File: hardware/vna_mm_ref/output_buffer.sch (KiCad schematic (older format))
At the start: 35 parts, among them J201 Conn_Coaxial, J202 Conn_Coaxial, U201 LTC6957xDD-3

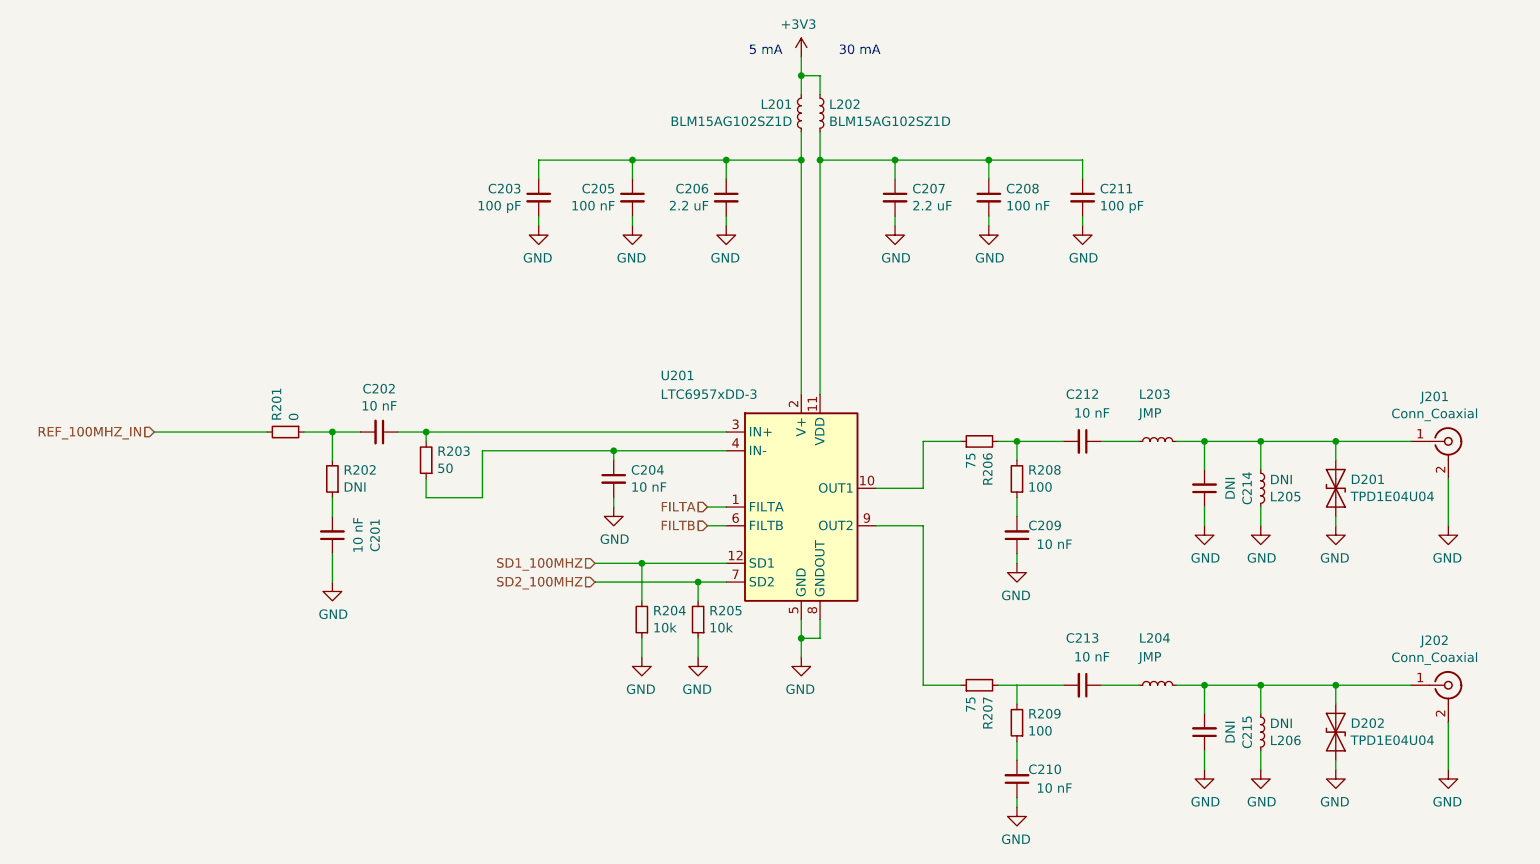
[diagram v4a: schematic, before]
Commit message: component placement on vna ref board
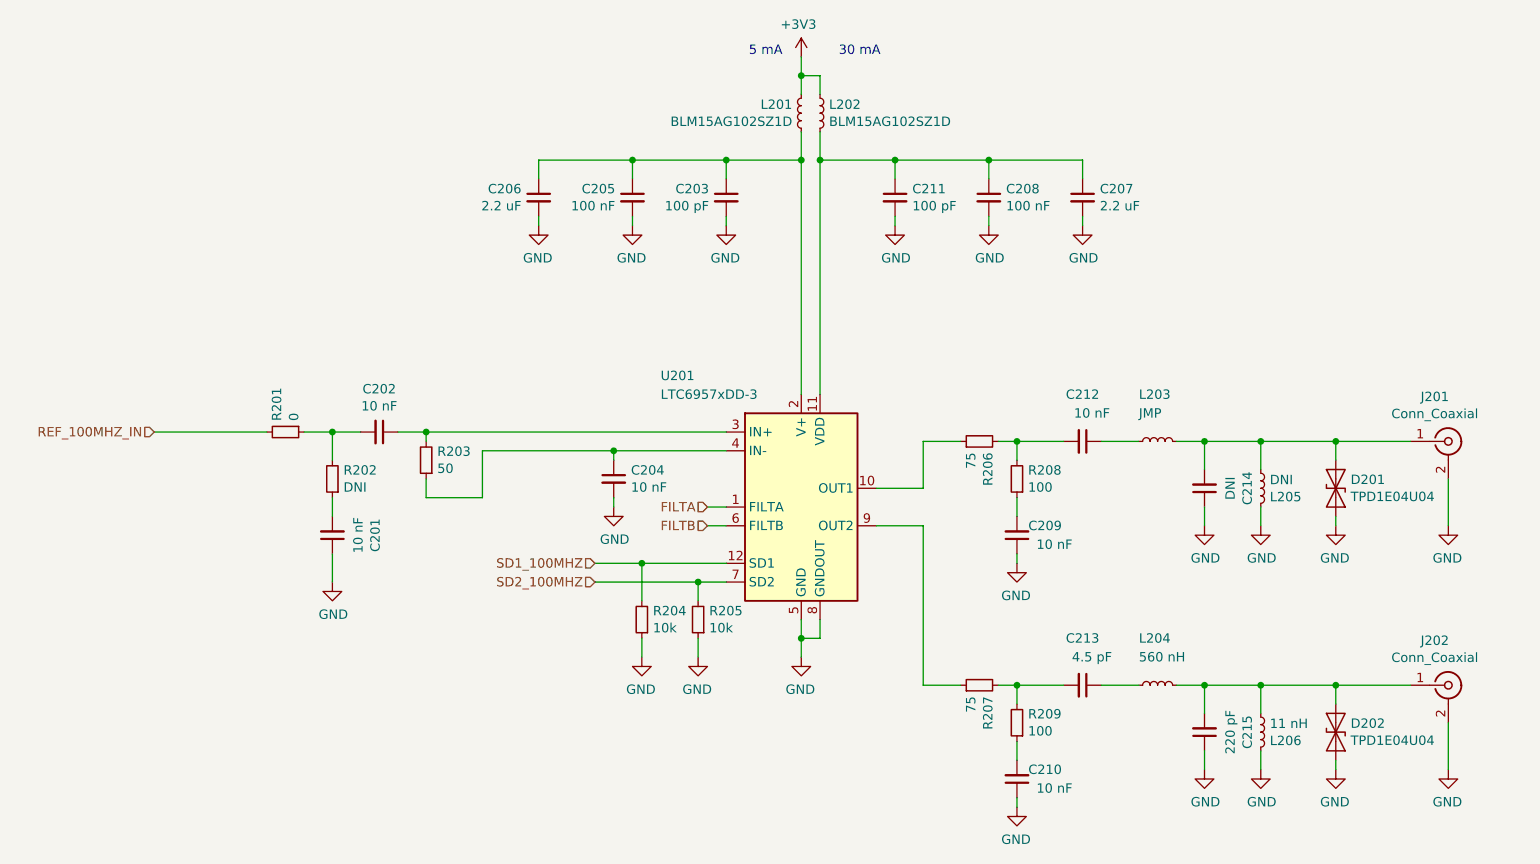
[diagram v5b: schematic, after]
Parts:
- C213: value 10 nF -> 4.5 pF
- C215: value DNI -> 220 pF
- L204: value JMP -> 560 nH
- L206: value DNI -> 11 nH
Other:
- moved on the sheet: C203, C206, C207, C211
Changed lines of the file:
@@
 L Device:C_Small C?
 U 1 1 5DBFE6FF
-P 3750 2100
+P 4750 2100
 AR Path="/5DBFE6FF" Ref="C?"  Part="1"
 AR Path="/5DBF0563/5DBFE6FF" Ref="C203"  Part="1"
-F 0 "C203" H 3842 2146 50  0000 L CNN
-F 1 "100 pF" H 3842 2055 50  0000 L CNN
-F 2 "Capacitor_SMD:C_0402_1005Metric" H 3750 2100 50  0001 C CNN
-F 3 "~" H 3750 2100 50  0001 C CNN
-	1    3750 2100
+F 0 "C203" H 4842 2146 50  0000 L CNN
+F 1 "100 pF" H 4842 2055 50  0000 L CNN
+F 2 "Capacitor_SMD:C_0402_1005Metric" H 4750 2100 50  0001 C CNN
+F 3 "~" H 4750 2100 50  0001 C CNN
+	1    4750 2100
 	-1   0    0    -1
 $EndComp
@@
 L Device:C_Small C?
 U 1 1 5DBFE70B
-P 4750 2100
+P 3750 2100
 AR Path="/5DBFE70B" Ref="C?"  Part="1"
 AR Path="/5DBF0563/5DBFE70B" Ref="C206"  Part="1"
-F 0 "C206" H 4842 2146 50  0000 L CNN
-F 1 "2.2 uF" H 4842 2055 50  0000 L CNN
-F 2 "Capacitor_SMD:C_0603_1608Metric" H 4750 2100 50  0001 C CNN
-F 3 "~" H 4750 2100 50  0001 C CNN
-	1    4750 2100
+F 0 "C206" H 3842 2146 50  0000 L CNN
+F 1 "2.2 uF" H 3842 2055 50  0000 L CNN
+F 2 "Capacitor_SMD:C_0603_1608Metric" H 3750 2100 50  0001 C CNN
+F 3 "~" H 3750 2100 50  0001 C CNN
+	1    3750 2100
 	-1   0    0    -1
 $EndComp
@@
 L Device:C_Small C?
 U 1 1 5DBFE754
-P 6650 2100
+P 5650 2100
 AR Path="/5DBFE754" Ref="C?"  Part="1"
 AR Path="/5DBF0563/5DBFE754" Ref="C211"  Part="1"
-F 0 "C211" H 6742 2146 50  0000 L CNN
-F 1 "100 pF" H 6742 2055 50  0000 L CNN
-F 2 "Capacitor_SMD:C_0402_1005Metric" H 6650 2100 50  0001 C CNN
-F 3 "~" H 6650 2100 50  0001 C CNN
-	1    6650 2100
+F 0 "C211" H 5742 2146 50  0000 L CNN
+F 1 "100 pF" H 5742 2055 50  0000 L CNN
+F 2 "Capacitor_SMD:C_0402_1005Metric" H 5650 2100 50  0001 C CNN
+F 3 "~" H 5650 2100 50  0001 C CNN
+	1    5650 2100
 	1    0    0    -1
 $EndComp
@@
 L Device:C_Small C?
 U 1 1 5DBFE760
-P 5650 2100
+P 6650 2100
 AR Path="/5DBFE760" Ref="C?"  Part="1"
 AR Path="/5DBF0563/5DBFE760" Ref="C207"  Part="1"
-F 0 "C207" H 5742 2146 50  0000 L CNN
-F 1 "2.2 uF" H 5742 2055 50  0000 L CNN
-F 2 "Capacitor_SMD:C_0603_1608Metric" H 5650 2100 50  0001 C CNN
-F 3 "~" H 5650 2100 50  0001 C CNN
-	1    5650 2100
+F 0 "C207" H 6742 2146 50  0000 L CNN
+F 1 "2.2 uF" H 6742 2055 50  0000 L CNN
+F 2 "Capacitor_SMD:C_0603_1608Metric" H 6650 2100 50  0001 C CNN
+F 3 "~" H 6650 2100 50  0001 C CNN
+	1    6650 2100
 	1    0    0    -1
 $EndComp
@@
 Wire Wire Line
 	6200 4700 6300 4700
-Wire Wire Line
-	6300 4800 6300 4700
 $Comp
 L Connector:Conn_Coaxial J?
@@
 AR Path="/5DBF0563/5DC92B18" Ref="C213"  Part="1"
 F 0 "C213" V 6400 4700 50  0000 C CNN
-F 1 "10 nF" V 6500 4750 50  0000 C CNN
+F 1 "4.5 pF" V 6500 4750 50  0000 C CNN
 F 2 "Capacitor_SMD:C_0402_1005Metric" H 6650 4700 50  0001 C CNN
 F 3 "~" H 6650 4700 50  0001 C CNN
@@
 AR Path="/5DBF0563/5DC92B1E" Ref="C215"  Part="1"
 F 0 "C215" V 7071 4950 50  0000 C CNN
-F 1 "DNI" V 7162 4950 50  0000 C CNN
+F 1 "220 pF" V 7162 4950 50  0000 C CNN
 F 2 "Capacitor_SMD:C_0402_1005Metric" H 7300 4950 50  0001 C CNN
 F 3 "~" H 7300 4950 50  0001 C CNN
@@
 AR Path="/5DC3C92E/5DC92B24" Ref="L?"  Part="1"
 F 0 "L204" V 7300 4600 50  0000 L CNN
-F 1 "JMP" V 7200 4600 50  0000 L CNN
+F 1 "560 nH" V 7200 4600 50  0000 L CNN
 F 2 "Inductor_SMD:L_0805_2012Metric" H 7050 4700 50  0001 C CNN
 F 3 "~" H 7050 4700 50  0001 C CNN
@@
 AR Path="/5DC3C92E/5DC92B2A" Ref="L?"  Part="1"
 F 0 "L206" H 7648 4996 50  0000 L CNN
-F 1 "DNI" H 7648 4905 50  0000 L CNN
+F 1 "11 nH" H 7648 4905 50  0000 L CNN
 F 2 "Inductor_SMD:L_0402_1005Metric" H 7600 4950 50  0001 C CNN
 F 3 "~" H 7600 4950 50  0001 C CNN
@@
 Wire Wire Line
 	8000 3400 8400 3400
+Wire Wire Line
+	6300 4800 6300 4700
+Connection ~ 6300 4700
 $EndSCHEMATC

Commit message: layout of 100 MHz reference board
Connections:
- net at U201.10 (OUT1): now also R207.1; no longer R206.1
- net at U201.9 (OUT2): now also R206.1; no longer R207.1
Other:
- moved on the sheet: C209, C210, C212, C213, C214, C215, D201, D202, J201, J202, L203, L204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

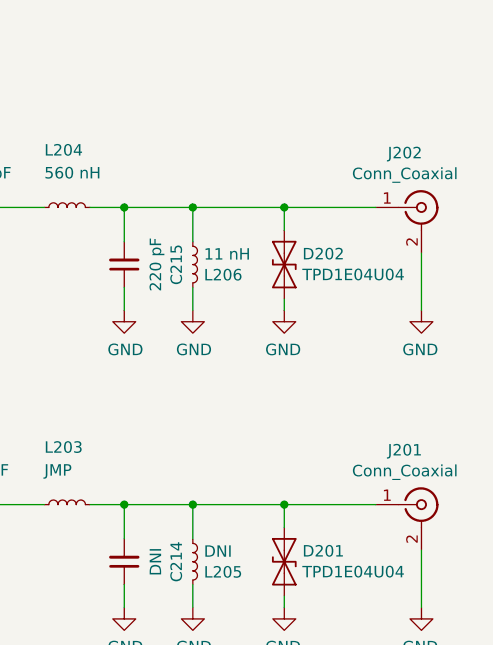
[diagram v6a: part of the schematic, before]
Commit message: created BOM for vna mm ref
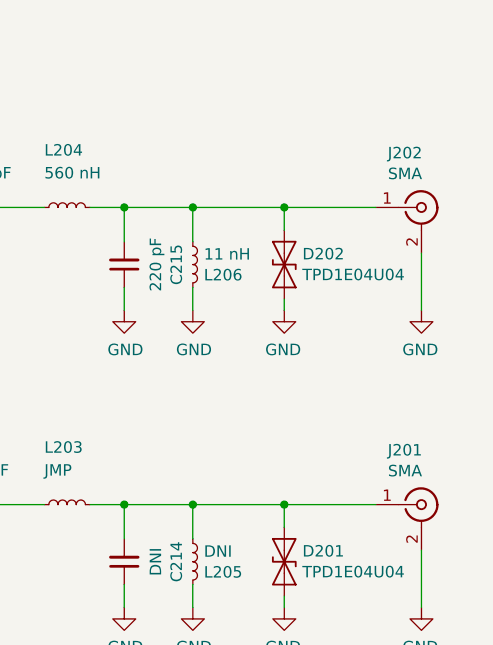
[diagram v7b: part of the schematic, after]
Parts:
- C206, C207: DIST_NAME (none) -> Digi-Key; DIST_PN (none) -> 490-10731-1-ND
- D201, D202: DIST_NAME (none) -> Digi-Key; DIST_PN (none) -> 296-47224-1-ND
- J201, J202: value Conn_Coaxial -> SMA; DIST_NAME (none) -> Digi-Key; DIST_PN (none) -> WM5534-ND
- L201, L202: DIST_NAME (none) -> Digi-Key; DIST_PN (none) -> BLM15AG102SZ1D
- L204: DIST_NAME (none) -> Digi-Key; DIST_PN (none) -> A103767CT-ND
- U201: DIST_NAME (none) -> Digi-Key; DIST_PN (none) -> LTC6957IDD-3#TRPBFCT-ND
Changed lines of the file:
@@
 F 2 "Package_DFN_QFN:DFN-12-1EP_3x3mm_P0.45mm_EP1.66x2.38mm" H 5150 3100 50  0001 C CNN
 F 3 "https://www.analog.com/media/en/technical-documentation/data-sheets/6957fb.pdf" H 5150 3750 50  0001 C CNN
+F 4 "Digi-Key" H 5150 3750 50  0001 C CNN "DIST_NAME"
+F 5 "LTC6957IDD-3#TRPBFCT-ND" H 5150 3750 50  0001 C CNN "DIST_PN"
 	1    5150 3750
 	1    0    0    -1
@@
 F 2 "Inductor_SMD:L_0402_1005Metric" H 5150 1650 50  0001 C CNN
 F 3 "~" H 5150 1650 50  0001 C CNN
+F 4 "Digi-Key" H 5150 1650 50  0001 C CNN "DIST_NAME"
+F 5 "BLM15AG102SZ1D" H 5150 1650 50  0001 C CNN "DIST_PN"
 	1    5150 1650
 	-1   0    0    -1
@@
 F 2 "Capacitor_SMD:C_0603_1608Metric" H 3750 2100 50  0001 C CNN
 F 3 "~" H 3750 2100 50  0001 C CNN
+F 4 "Digi-Key" H 3750 2100 50  0001 C CNN "DIST_NAME"
+F 5 "490-10731-1-ND" H 3750 2100 50  0001 C CNN "DIST_PN"
 	1    3750 2100
 	-1   0    0    -1
@@
 F 2 "Inductor_SMD:L_0402_1005Metric" H 5250 1650 50  0001 C CNN
 F 3 "~" H 5250 1650 50  0001 C CNN
+F 4 "Digi-Key" H 5250 1650 50  0001 C CNN "DIST_NAME"
+F 5 "BLM15AG102SZ1D" H 5250 1650 50  0001 C CNN "DIST_PN"
 	1    5250 1650
 	1    0    0    -1
@@
 F 2 "Capacitor_SMD:C_0603_1608Metric" H 6650 2100 50  0001 C CNN
 F 3 "~" H 6650 2100 50  0001 C CNN
+F 4 "Digi-Key" H 6650 2100 50  0001 C CNN "DIST_NAME"
+F 5 "490-10731-1-ND" H 6650 2100 50  0001 C CNN "DIST_PN"
 	1    6650 2100
 	1    0    0    -1
@@
 AR Path="/5DBF0563/5DBFE7CD" Ref="J201"  Part="1"
 F 0 "J201" H 8528 4938 50  0000 C CNN
-F 1 "Conn_Coaxial" H 8528 4847 50  0000 C CNN
+F 1 "SMA" H 8528 4847 50  0000 C CNN
 F 2 "Connector_Coaxial:SMA_Amphenol_132289_EdgeMount" H 8600 4700 50  0001 C CNN
 F 3 " ~" H 8600 4700 50  0001 C CNN
+F 4 "Digi-Key" H 8600 4700 50  0001 C CNN "DIST_NAME"
+F 5 "WM5534-ND" H 8600 4700 50  0001 C CNN "DIST_PN"
 	1    8600 4700
 	1    0    0    -1
@@
 F 2 "Diode_SMD:D_0402_1005Metric" H 8000 4950 50  0001 C CNN
 F 3 "~" H 8000 4950 50  0001 C CNN
+F 4 "Digi-Key" H 8000 4950 50  0001 C CNN "DIST_NAME"
+F 5 "296-47224-1-ND" H 8000 4950 50  0001 C CNN "DIST_PN"
 	1    8000 4950
 	0    1    1    0
@@
 AR Path="/5DBF0563/5DC92B00" Ref="J202"  Part="1"
 F 0 "J202" H 8528 3638 50  0000 C CNN
-F 1 "Conn_Coaxial" H 8528 3547 50  0000 C CNN
+F 1 "SMA" H 8528 3547 50  0000 C CNN
 F 2 "Connector_Coaxial:SMA_Amphenol_132289_EdgeMount" H 8600 3400 50  0001 C CNN
 F 3 " ~" H 8600 3400 50  0001 C CNN
+F 4 "Digi-Key" H 8600 3400 50  0001 C CNN "DIST_NAME"
+F 5 "WM5534-ND" H 8600 3400 50  0001 C CNN "DIST_PN"
 	1    8600 3400
 	1    0    0    -1
@@
 F 2 "Diode_SMD:D_0402_1005Metric" H 8000 3650 50  0001 C CNN
 F 3 "~" H 8000 3650 50  0001 C CNN
+F 4 "Digi-Key" H 8000 3650 50  0001 C CNN "DIST_NAME"
+F 5 "296-47224-1-ND" H 8000 3650 50  0001 C CNN "DIST_PN"
 	1    8000 3650
 	0    1    1    0
@@
 F 2 "Inductor_SMD:L_0805_2012Metric" H 7050 3400 50  0001 C CNN
 F 3 "~" H 7050 3400 50  0001 C CNN
+F 4 "Digi-Key" H 7050 3400 50  0001 C CNN "DIST_NAME"
+F 5 "A103767CT-ND" H 7050 3400 50  0001 C CNN "DIST_PN"
 	1    7050 3400
 	0    1    -1   0
